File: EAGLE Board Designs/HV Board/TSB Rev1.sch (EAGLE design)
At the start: 149 parts, among them J3 CONNECTOR-8_MF_T_V_, J5 CONNECTOR-4__, K4 RELAY_SPST_NC_POLARIZED_3550_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, K5 RELAY_SPST_NO_3550_12, Q2 TRANSISTOR_N_MOS__PMV15ENEA, U1 LTC6994_1, U10 DCM4623TD2J13D0T70, U11 RELAY_SOLIDSTATE_NC_AG, U15 LOGICGATE_INVERTER_DCKR, U16 LTC3639, U17 VOLTAGE_REGULATOR_ADJ_LR8_SOT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, U18 ISO224B_AIRGAP, U19 ISO224B_AIRGAP, U2 VOLTAGE_REGULATOR_SOT223_5V

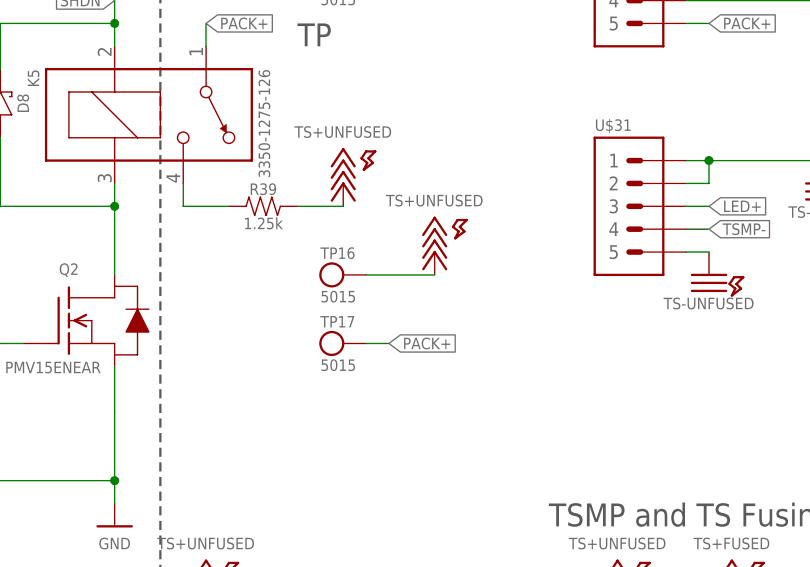
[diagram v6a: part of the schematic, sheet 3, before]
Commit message: All routed except for tps
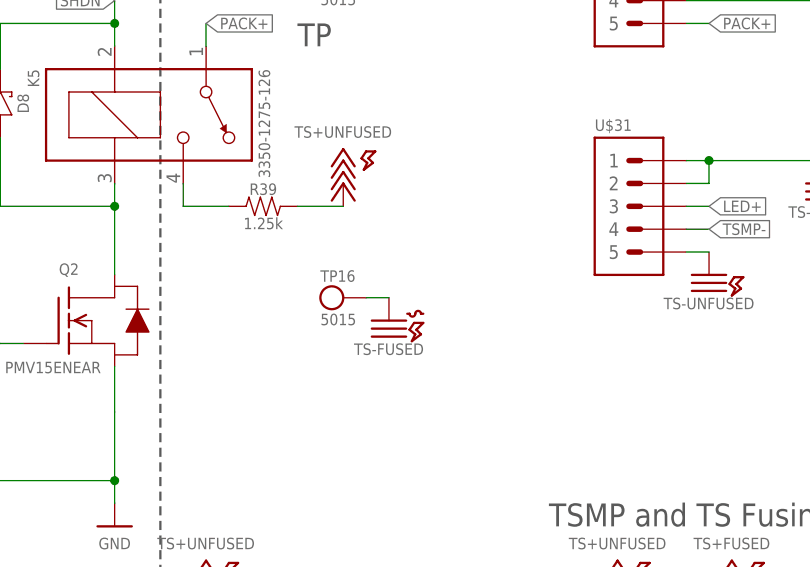
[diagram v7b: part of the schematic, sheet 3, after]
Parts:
- removed TP17: TEST_POINT, HyTechDevices:TEST_POINT
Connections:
- net PACK+: no longer TP17.P$1
- net TS+UNFUSED: no longer TP16.P$1
- net TS-FUSED: now also TP16.P$1
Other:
- moved on the sheet: TP16
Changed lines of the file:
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@@
 <part name="D12" library="HyTechDevices" deviceset="LED_?_*" device="0603" technology="WHITE"/>
 <part name="P7" library="HyTechSupplies" deviceset="GND" device=""/>
-<part name="TP16" library="HyTechDevices" deviceset="TEST_POINT" device=""/>
-<part name="TP17" library="HyTechDevices" deviceset="TEST_POINT" device=""/>
-<part name="P13" library="HyTechSupplies" deviceset="TS+UNFUSED" device=""/>
 <part name="TP18" library="HyTechDevices" deviceset="TEST_POINT" device=""/>
 <part name="TP19" library="HyTechDevices" deviceset="TEST_POINT" device=""/>
@@
 <part name="U$33" library="HyTechDevices" deviceset="CONNECTOR-5_?_*" device="7_SPACED"/>
 <part name="P18" library="HyTechSupplies" deviceset="+5V" device=""/>
+<part name="TP16" library="HyTechDevices" deviceset="TEST_POINT" device=""/>
+<part name="U$42" library="HyTechSupplies" deviceset="TS-FUSED" device=""/>
 </parts>
 <sheets>
@@
 <attribute name="VALUE" x="88.9" y="138.43" size="1.27" layer="96" align="top-center"/>
 </instance>
-<instance part="TP16" gate="G$1" x="203.2" y="139.7" smashed="yes">
-<attribute name="NAME" x="200.66" y="141.478" size="1.27" layer="95"/>
-<attribute name="MPN" x="200.66" y="137.922" size="1.27" layer="95" align="top-left"/>
-</instance>
-<instance part="TP17" gate="G$1" x="203.2" y="132.08" smashed="yes">
-<attribute name="NAME" x="200.66" y="133.858" size="1.27" layer="95"/>
-<attribute name="MPN" x="200.66" y="130.302" size="1.27" layer="95" align="top-left"/>
-</instance>
-<instance part="P13" gate="G$1" x="213.36" y="142.24" smashed="yes">
-<attribute name="VALUE" x="213.36" y="147.32" size="1.27" layer="96" align="bottom-center"/>
-</instance>
 <instance part="TP18" gate="G$1" x="251.46" y="88.9" smashed="yes" rot="R180">
 <attribute name="NAME" x="254" y="87.122" size="1.27" layer="95" rot="R180"/>
@@
 <instance part="U$33" gate="G$1" x="231.14" y="180.34" smashed="yes">
 <attribute name="NAME" x="231.14" y="181.102" size="1.27" layer="95"/>
+</instance>
+<instance part="TP16" gate="G$1" x="203.2" y="137.16" smashed="yes">
+<attribute name="NAME" x="200.66" y="138.938" size="1.27" layer="95"/>
+<attribute name="MPN" x="200.66" y="135.382" size="1.27" layer="95" align="top-left"/>
+</instance>
+<instance part="U$42" gate="G$1" x="208.28" y="134.62" smashed="yes">
+<attribute name="VALUE" x="208.28" y="132.08" size="1.27" layer="96" align="top-center"/>
 </instance>
 </instances>
@@
 </segment>
 <segment>
-<pinref part="TP16" gate="G$1" pin="P$1"/>
-<wire x1="205.74" y1="139.7" x2="213.36" y2="139.7" width="0.6096" layer="91"/>
-<pinref part="P13" gate="G$1" pin="TS+UNFUSED"/>
-</segment>
-<segment>
 <pinref part="P14" gate="G$1" pin="TS+UNFUSED"/>
 <wire x1="241.3" y1="177.8" x2="246.38" y2="177.8" width="0.6096" layer="91"/>
@@
 <wire x1="205.74" y1="180.34" x2="208.28" y2="180.34" width="0.6096" layer="91"/>
 <label x="208.28" y="180.34" size="1.27" layer="95" xref="yes"/>
-</segment>
-<segment>
-<pinref part="TP17" gate="G$1" pin="P$1"/>
-<wire x1="205.74" y1="132.08" x2="208.28" y2="132.08" width="0.6096" layer="91"/>
-<label x="208.28" y="132.08" size="1.27" layer="95" xref="yes"/>
 </segment>
 </net>
@@
 <junction x="243.84" y="152.4"/>
 </segment>
-</net>
+<segment>
+<pinref part="TP16" gate="G$1" pin="P$1"/>
+<wire x1="205.74" y1="137.16" x2="208.28" y2="137.16" width="0.1524" layer="91"/>
+<pinref part="U$42" gate="G$1" pin="TS-FUSED"/>
+</segment>
+</net>

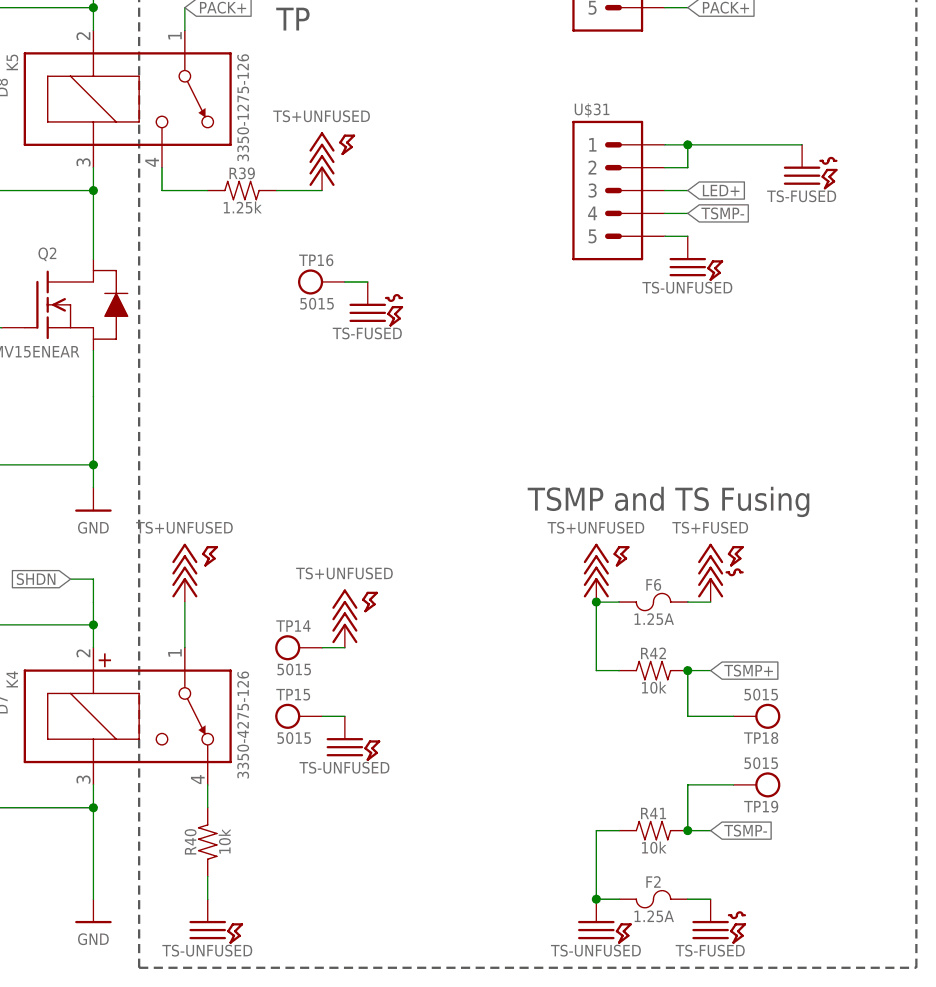
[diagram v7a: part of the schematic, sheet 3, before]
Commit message: Added silkscreen and fixed some parts
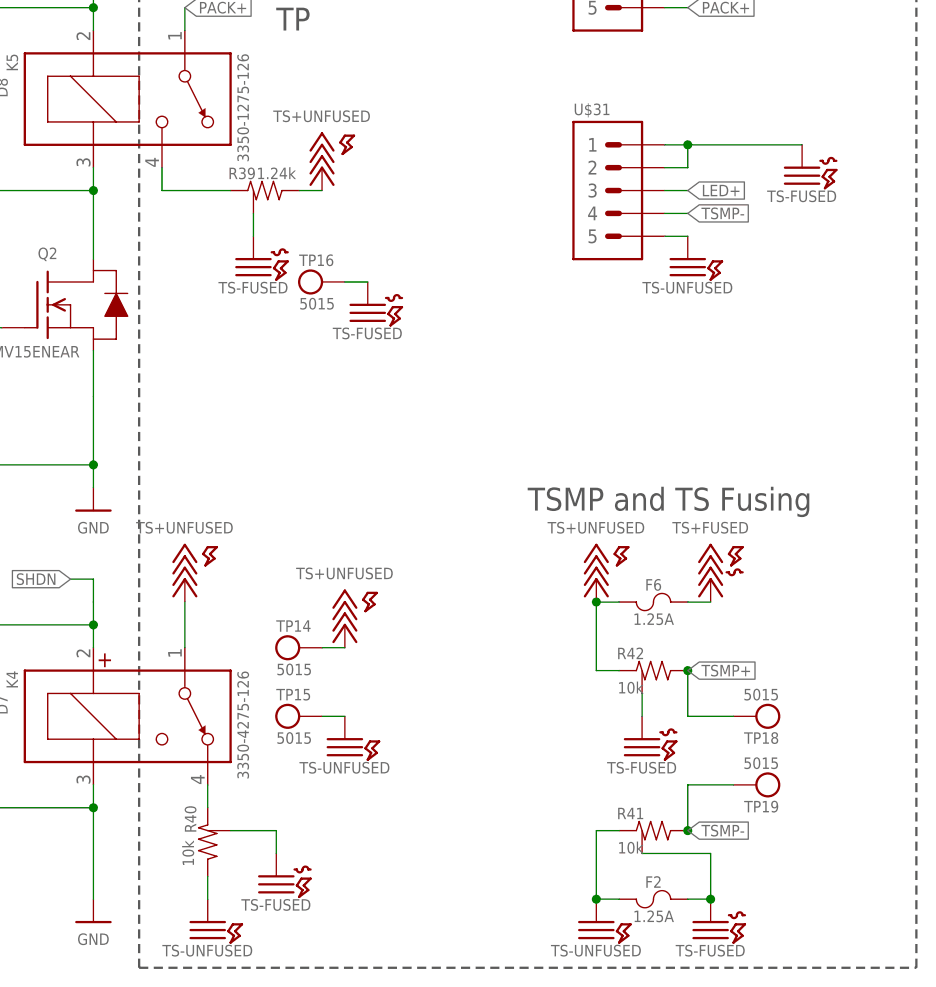
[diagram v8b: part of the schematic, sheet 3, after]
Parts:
- R39: value RESISTOR_B20_1.25K -> RESISTOR_GND_1.24K; device HyTechDevices:RESISTOR_B20_1.25K -> HyTechDevices:RESISTOR_GND_1.24K
- R40, R41, R42: value RESISTOR_B20_10K -> RESISTOR_GND_10K; device HyTechDevices:RESISTOR_B20_10K -> HyTechDevices:RESISTOR_GND_10K
- U17: value VOLTAGE_REGULATOR_ADJ_LR8_SOT89 -> VOLTAGE_REGULATOR_ADJ_LR8_DPAK; device HyTechDevices:VOLTAGE_REGULATOR_ADJ_LR8_SOT89 -> HyTechDevices:VOLTAGE_REGULATOR_ADJ_LR8_DPAK
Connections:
- net TS-FUSED: now also R39.3, R40.3, R41.3, R42.3
